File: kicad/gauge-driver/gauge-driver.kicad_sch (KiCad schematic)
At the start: 19 parts, among them J1 Conn_01x02_Socket, U1 ESP32-WROOM-32E, U2 SN65HVD230, U3 LM2675M-3.3, Y1 Crystal

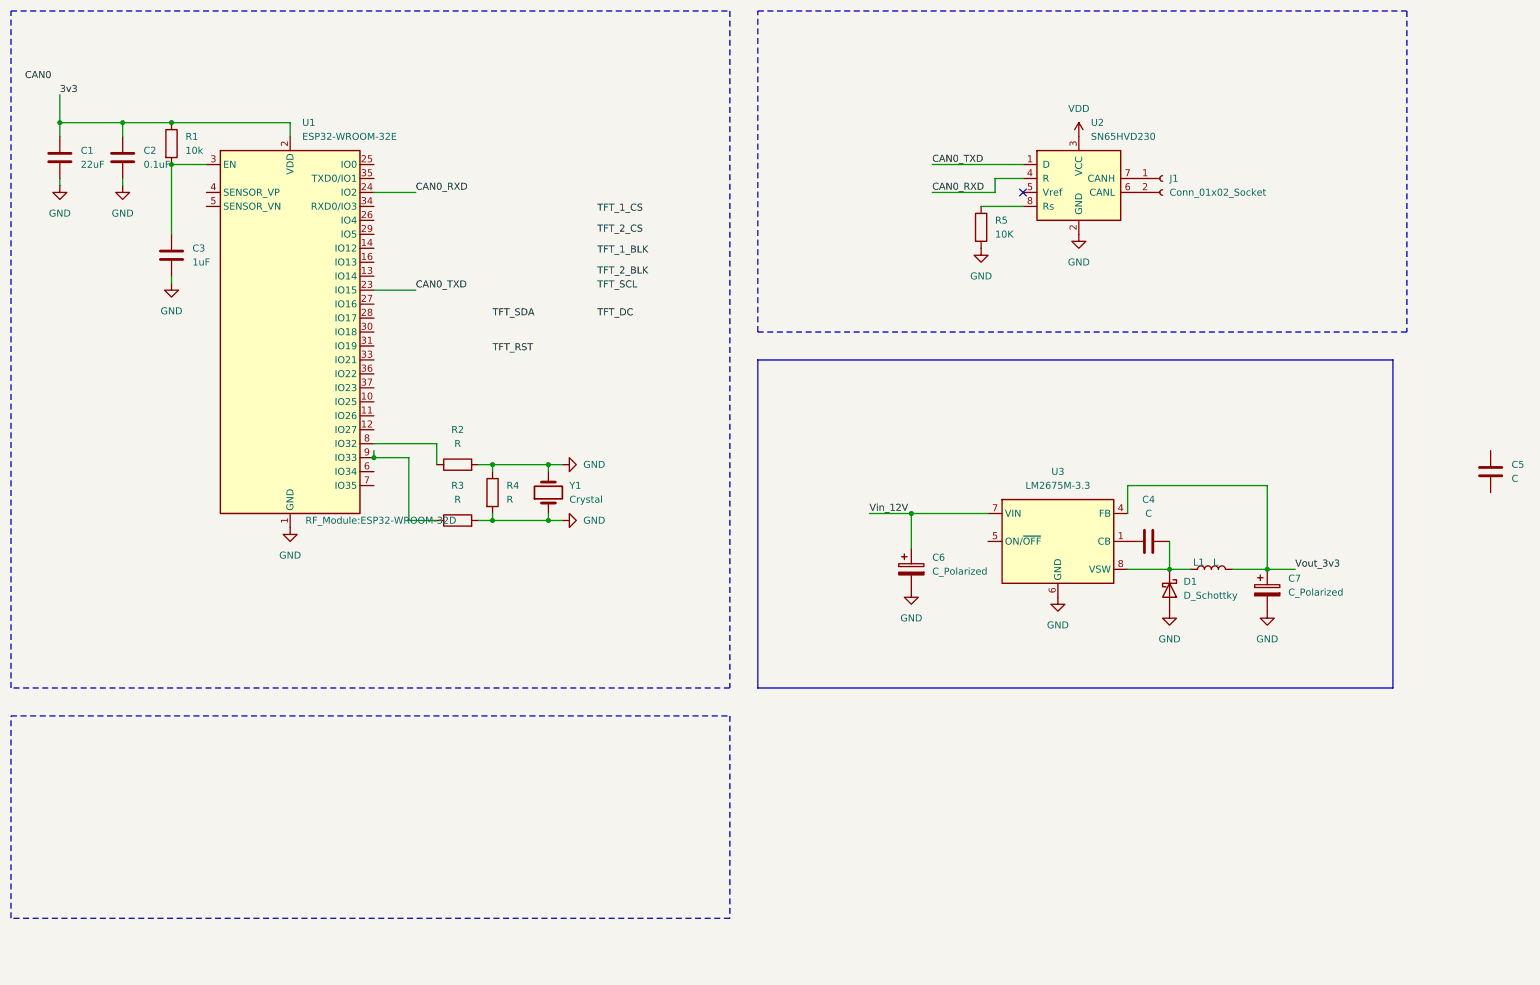
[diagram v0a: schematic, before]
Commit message: Added cp2102
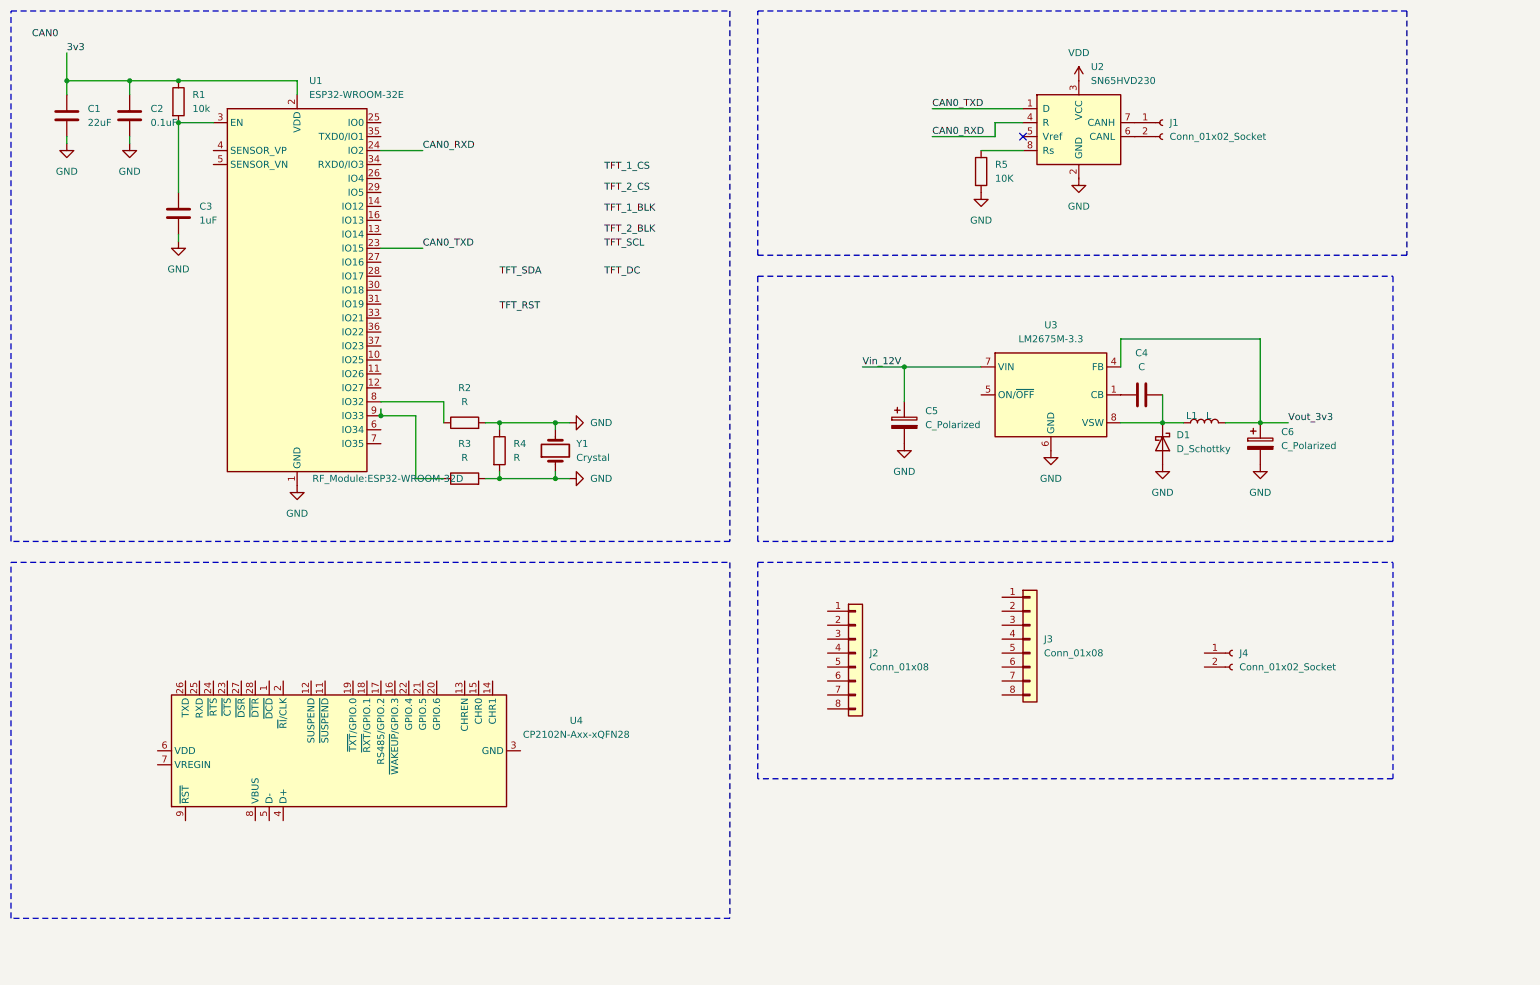
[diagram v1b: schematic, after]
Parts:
- removed C5: C, symbol Device:C
- added J2: Conn_01x08, Connector_PinSocket_2.54mm:PinSocket_1x08_P2.54mm_Vertical, symbol Connector_Generic:Conn_01x08
- added J3: Conn_01x08, symbol Connector_Generic:Conn_01x08
- added J4: Conn_01x02_Socket, symbol Connector:Conn_01x02_Socket
- added U4: CP2102N-Axx-xQFN28, Package_DFN_QFN:QFN-28-1EP_5x5mm_P0.5mm_EP3.35x3.35mm, symbol Interface_USB:CP2102N-Axx-xQFN28
- C4: footprint (none) -> Capacitor_SMD:C_0603_1608Metric
- C5: renamed from C6; footprint (none) -> Capacitor_SMD:CP_Elec_6.3x3
- C6: renamed from C7; footprint (none) -> Capacitor_SMD:CP_Elec_6.3x3
- D1: footprint (none) -> Diode_SMD:D_2114_3652Metric
- J1: footprint (none) -> Connector_PinSocket_2.54mm:PinSocket_1x02_P2.54mm_Vertical
- L1: footprint (none) -> Inductor_SMD:L_0603_1608Metric
- R5: footprint (none) -> Resistor_SMD:R_0603_1608Metric
- Y1: footprint (none) -> Crystal:Crystal_HC18-U_Vertical
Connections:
- new net: U4.29 (GND), U4.3 (GND)
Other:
- moved on the sheet: C1, C2, C3, C4, C5, C6, D1, J1, L1, R1, R2, R3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

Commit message: updated cp2102 wiring
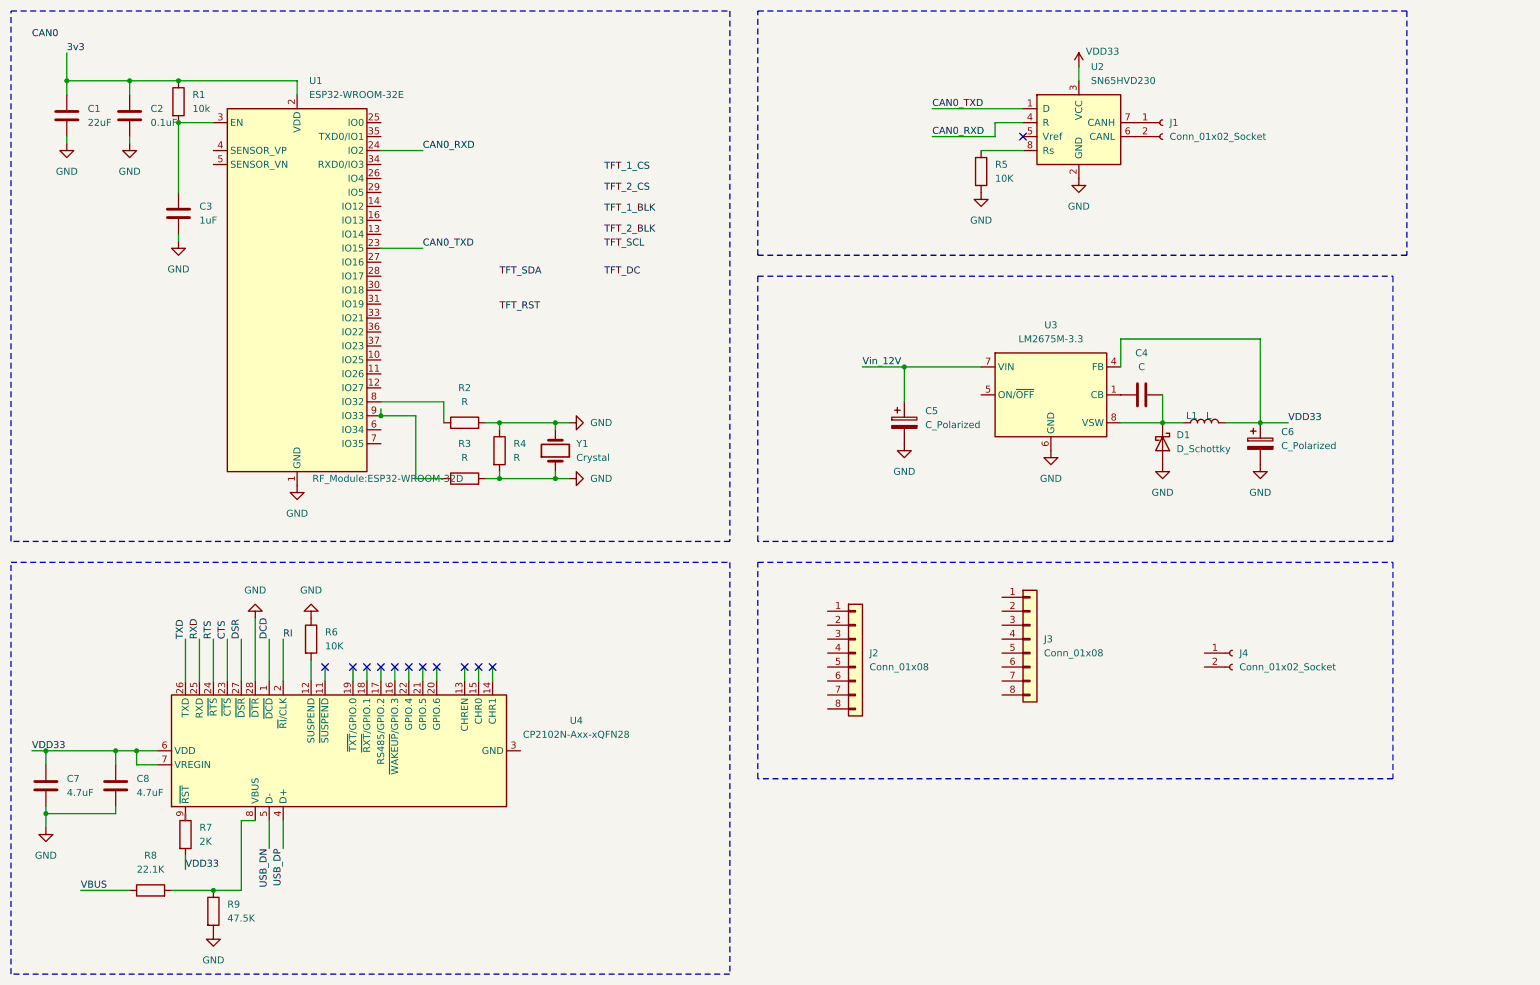
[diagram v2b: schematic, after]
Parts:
- added C7, C8: 4.7uF, symbol Device:C
- added R6: 10K, symbol Device:R
- added R7: 2K, symbol Device:R
- added R8: 22.1K, symbol Device:R
- added R9: 47.5K, symbol Device:R
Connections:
- net VDD is gone; now on net VDD33: U2.3 (VCC)
- net Vout_3v3 is gone; now on net VDD33: C6.1, L1.2, U3.4 (FB)
- net GND: now also U4.28 (~{DTR}), C7.2, C8.2, R6.1, R9.2
- net DCD: now reaches U4.1 (~{DCD})
- net at U4.12 (SUSPEND): now also R6.2
- net RI: now reaches U4.2 (~{RI}/CLK)
- net CTS: now reaches U4.23 (~{CTS})
- net RTS: now reaches U4.24 (~{RTS})
- net RXD: now reaches U4.25 (RXD)
- net TXD: now reaches U4.26 (TXD)
- net DSR: now reaches U4.27 (~{DSR})
- net USB_DP: now reaches U4.4 (D+)
- net USB_DN: now reaches U4.5 (D-)
- net VDD33: now reaches U4.6 (VDD)
- net VDD33: now also U4.7 (VREGIN), C7.1, C8.1, R7.2
- net at U4.8 (VBUS): now also R8.2, R9.1
- net at U4.9 (~{RST}): now also R7.1
- new net VBUS: R8.1
- no-connect marks 1 -> 12

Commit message: kicad
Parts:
- C7, C8: footprint (none) -> Capacitor_SMD:C_0603_1608Metric
- J3: footprint (none) -> Connector_PinHeader_2.54mm:PinHeader_1x08_P2.54mm_Vertical
- J4: footprint (none) -> Connector_PinHeader_2.54mm:PinHeader_1x02_P2.54mm_Vertical
- R6, R7, R8, R9: footprint (none) -> Resistor_SMD:R_0603_1608Metric
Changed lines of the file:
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@@
 			)
 		)
-		(property "Footprint" ""
+		(property "Footprint" "Capacitor_SMD:C_0603_1608Metric"
 			(at 30.1752 166.37 0)
 			(effects
@@
 			)
 		)
-		(property "Footprint" ""
+		(property "Footprint" "Connector_PinHeader_2.54mm:PinHeader_1x08_P2.54mm_Vertical"
 			(at 208.28 135.89 0)
 			(effects
@@
 			)
 		)
-		(property "Footprint" ""
+		(property "Footprint" "Resistor_SMD:R_0603_1608Metric"
 			(at 75.692 135.89 90)
 			(effects
@@
 			)
 		)
-		(property "Footprint" ""
+		(property "Footprint" "Connector_PinHeader_2.54mm:PinHeader_1x02_P2.54mm_Vertical"
 			(at 245.11 138.43 0)
 			(effects
@@
 			)
 		)
-		(property "Footprint" ""
+		(property "Footprint" "Capacitor_SMD:C_0603_1608Metric"
 			(at 42.8752 166.37 0)
 			(effects
@@
 			)
 		)
-		(property "Footprint" ""
+		(property "Footprint" "Resistor_SMD:R_0603_1608Metric"
 			(at 57.912 185.42 90)
 			(effects
@@
 			)
 		)
-		(property "Footprint" ""
+		(property "Footprint" "Resistor_SMD:R_0603_1608Metric"
 			(at 48.26 183.388 90)
 			(effects
@@
 			)
 		)
-		(property "Footprint" ""
+		(property "Footprint" "Resistor_SMD:R_0603_1608Metric"
 			(at 52.832 171.45 90)
 			(effects

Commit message: Fixed re-ordering. Both screens now loading logo
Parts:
- C7, C8: footprint Capacitor_SMD:C_0603_1608Metric -> (none)
- J3: footprint Connector_PinHeader_2.54mm:PinHeader_1x08_P2.54mm_Vertical -> (none)
- J4: footprint Connector_PinHeader_2.54mm:PinHeader_1x02_P2.54mm_Vertical -> (none)
- R6, R7, R8, R9: footprint Resistor_SMD:R_0603_1608Metric -> (none)
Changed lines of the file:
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@@
 			)
 		)
-		(property "Footprint" "Capacitor_SMD:C_0603_1608Metric"
+		(property "Footprint" ""
 			(at 30.1752 166.37 0)
 			(effects
@@
 			)
 		)
-		(property "Footprint" "Connector_PinHeader_2.54mm:PinHeader_1x08_P2.54mm_Vertical"
+		(property "Footprint" ""
 			(at 208.28 135.89 0)
 			(effects
@@
 			)
 		)
-		(property "Footprint" "Resistor_SMD:R_0603_1608Metric"
+		(property "Footprint" ""
 			(at 75.692 135.89 90)
 			(effects
@@
 			)
 		)
-		(property "Footprint" "Connector_PinHeader_2.54mm:PinHeader_1x02_P2.54mm_Vertical"
+		(property "Footprint" ""
 			(at 245.11 138.43 0)
 			(effects
@@
 			)
 		)
-		(property "Footprint" "Capacitor_SMD:C_0603_1608Metric"
+		(property "Footprint" ""
 			(at 42.8752 166.37 0)
 			(effects
@@
 			)
 		)
-		(property "Footprint" "Resistor_SMD:R_0603_1608Metric"
+		(property "Footprint" ""
 			(at 57.912 185.42 90)
 			(effects
@@
 			)
 		)
-		(property "Footprint" "Resistor_SMD:R_0603_1608Metric"
+		(property "Footprint" ""
 			(at 48.26 183.388 90)
 			(effects
@@
 			)
 		)
-		(property "Footprint" "Resistor_SMD:R_0603_1608Metric"
+		(property "Footprint" ""
 			(at 52.832 171.45 90)
 			(effects
